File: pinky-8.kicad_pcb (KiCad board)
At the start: 2 copper layers, 91.4 x 68.6 mm, 21 parts, among them P1 USB_B, P2 PERIPHERAL A, P3 PERIPHERAL B, P4 2x3 HEADER, U1 W65C02S, U2 74AC00, U3 AS6C62256, U4 DS1813, U5 GLS29EE010, U6 W65C22S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

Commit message: Updating to Rev B spec.
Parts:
- removed C2: 100uF, Capacitors_THT:CP_Radial_D6.3mm_P2.50mm
- removed the G*** at (118.1, 66.0)
- removed R4, R5: 3.3K, Resistors_THT:R_Axial_DIN0204_L3.6mm_D1.6mm_P7.62mm_Horizontal
- removed the REF** at (110.5, 123.2)
- removed the REF** at (191.8, 81.3)
- removed the REF** at (110.5, 64.8)
- removed U1: W65C02S, Housings_DIP:DIP-40_W15.24mm_LongPads
- removed U2: 74AC00, Housings_DIP:DIP-14_W7.62mm_LongPads
- removed U3: AS6C62256, Housings_DIP:DIP-28_W15.24mm_LongPads
- removed U4: DS1813, TO_SOT_Packages_THT:TO-92_Inline_Wide
- removed U5: GLS29EE010, Housings_DIP:DIP-32_W15.24mm_Socket_LongPads
- removed X1: MXO45, Housings_DIP:DIP-8_W7.62mm_Socket_LongPads
- added B0: CONN_01X03, Pin_Headers:Pin_Header_Straight_1x03_Pitch2.54mm, F.Cu at (139.7, 31.8)
- added B1: CONN_01X03, Pin_Headers:Pin_Header_Straight_1x03_Pitch2.54mm, F.Cu at (135.9, 31.8)
- added B2: CONN_01X03, Pin_Headers:Pin_Header_Straight_1x03_Pitch2.54mm, F.Cu at (132.1, 31.8)
- added C7: 100uF, Capacitors_THT:CP_Radial_D6.3mm_P2.50mm, F.Cu at (157.5, 31.8)
- added CPU: W65C02S, Housings_DIP:DIP-40_W15.24mm_LongPads, F.Cu at (113.0, 44.5)
- added DEC: 74AC00, Housings_DIP:DIP-14_W7.62mm_LongPads, F.Cu at (132.1, 49.5)
- added G***: OSHW-logo_silkscreen-front_8mm, OSHW-logo:OSHW-logo_silkscreen-front_8mm, F.Cu at (87.0, 62.2)
- added NMI: SW_Push_Dual, Buttons_Switches_THT:SW_TH_Tactile_Omron_B3F-10xx, F.Cu at (101.6, 30.5)
- added OSC: MXO45, Housings_DIP:DIP-8_W7.62mm_Socket_LongPads, F.Cu at (114.3, 30.5)
- added P10: CONN_01X01, Wire_Pads:SolderWirePad_single_0-8mmDrill, F.Cu at (135.3, 92.1)
- added P11: CONN_01X01, Wire_Pads:SolderWirePad_single_0-8mmDrill, F.Cu at (154.3, 87.6)
- added P13: CONN_01X01, Wire_Pads:SolderWirePad_single_0-8mmDrill, F.Cu at (124.5, 91.4)
- added P14: CONN_01X01, Wire_Pads:SolderWirePad_single_0-8mmDrill, F.Cu at (144.1, 54.0)
- added P15: CONN_01X01, Wire_Pads:SolderWirePad_single_0-8mmDrill, F.Cu at (116.8, 61.0)
- added P17: CONN_01X01, Wire_Pads:SolderWirePad_single_0-8mmDrill, F.Cu at (97.2, 44.5)
- added P5: CONN_01X01, Wire_Pads:SolderWirePad_single_0-8mmDrill, F.Cu at (147.3, 46.4)
- added P6: CONN_01X01, Wire_Pads:SolderWirePad_single_0-8mmDrill, F.Cu at (163.2, 54.6)
- added PA: PERIPHERAL A, Socket_Strips:Socket_Strip_Straight_2x07_Pitch2.54mm, F.Cu at (87.6, 36.8)
- added PB: PERIPHERAL B, Socket_Strips:Socket_Strip_Straight_2x07_Pitch2.54mm, F.Cu at (87.6, 72.4)
- added R3: 3.3K, Resistors_THT:R_Axial_DIN0204_L3.6mm_D1.6mm_P7.62mm_Horizontal, F.Cu at (128.3, 38.1)
- added RAM: AS6C62256, Housings_DIP:DIP-28_W15.24mm_LongPads, F.Cu at (166.4, 87.6)
- added REF**: MountingHole_2.7mm_M2.5, Mounting_Holes:MountingHole_2.7mm_M2.5, F.Cu at (165.7, 31.1)
- added REF**: MountingHole_2.7mm_M2.5, Mounting_Holes:MountingHole_2.7mm_M2.5, F.Cu at (165.7, 93.3)
- added REF**: MountingHole_2.7mm_M2.5, Mounting_Holes:MountingHole_2.7mm_M2.5, F.Cu at (85.7, 93.3)
- added REF**: MountingHole_2.7mm_M2.5, Mounting_Holes:MountingHole_2.7mm_M2.5, F.Cu at (85.7, 31.1)
- added ROM: GLS29EE010, Housings_DIP:DIP-32_W15.24mm_Socket_LongPads, F.Cu at (147.3, 92.7)
- added U7: DS1813, TO_SOT_Packages_THT:TO-92_Inline_Wide, F.Cu at (151.1, 35.6)
- added USB-B: USB_B, Connectors:USB_B, F.Cu at (154.9, 43.2)
- added VIA: W65C22S, Housings_DIP:DIP-40_W15.24mm_LongPads, F.Cu at (94.0, 44.5)
- P1: value USB_B -> CONN_01X01; footprint Connectors:USB_B -> Wire_Pads:SolderWirePad_single_0-8mmDrill
- P2: value PERIPHERAL A -> CONN_01X01; footprint Socket_Strips:Socket_Strip_Straight_2x07_Pitch2.54mm -> Wire_Pads:SolderWirePad_single_0-8mmDrill
- P3: value PERIPHERAL B -> CONN_01X01; footprint Socket_Strips:Socket_Strip_Straight_2x07_Pitch2.54mm -> Wire_Pads:SolderWirePad_single_0-8mmDrill
- P4: value 2x3 HEADER -> CONN_01X01; footprint Pin_Headers:Pin_Header_Straight_2x03_Pitch2.54mm -> Wire_Pads:SolderWirePad_single_0-8mmDrill
- U6: value W65C22S -> DS1813; footprint Housings_DIP:DIP-40_W15.24mm_LongPads -> TO_SOT_Packages_THT:TO-92_Inline_Wide
- moved P1 77.8 mm to (118.1, 30.5)
- moved P4 75.4 mm to (118.1, 38.1), turned to 0 degrees
- moved R1 60.2 mm to (110.5, 30.5), turned to 270 degrees
- moved U6 41.9 mm to (106.7, 35.6), turned to 90 degrees
- moved RESET 40.2 mm to (147.3, 30.5), turned to 270 degrees
- moved P2 34.0 mm to (132.1, 45.1)
- moved R2 29.0 mm to (125.7, 38.1), turned to 90 degrees
- moved P3 16.5 mm to (97.2, 92.7)
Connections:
- P4 pad 1: Net-(P4-Pad1) -> GND
- R1 pad 1: Net-(R1-Pad1) -> VCC
- R1 pad 2: VCC -> Net-(R1-Pad2)
- R2 pad 1: VCC -> /PLUP
- R2 pad 2: Net-(R2-Pad2) -> VCC
- RESET pad 4: /RST -> /RST#
- U6 pad 1: GND -> /NMI#
- U6 pad 2: /PA0 -> VCC
- U6 pad 3: /PA1 -> GND
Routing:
- net /RW#: track 0.00 -> 124.9 mm, vias 0 -> 5
- net /RB2: track 0.00 -> 88.2 mm, vias 0 -> 1
- net /RW: track 83.6 -> 0.00 mm, vias 1 -> 0
- net /CLK: track 17.6 -> 99.5 mm
- net /VIASEL: track 78.7 -> 0.00 mm, vias 2 -> 0
- net /VIASEL#: track 0.00 -> 75.6 mm, vias 0 -> 2
- net /PHI2: track 65.7 -> 0.00 mm
- net /RST#: track 0.00 -> 59.7 mm, vias 0 -> 1
- net /ROMSEL#: track 0.00 -> 58.8 mm, vias 0 -> 2
- net /IRQ#: track 0.00 -> 57.8 mm, vias 0 -> 1
- net /RST: track 56.1 -> 0.00 mm, vias 3 -> 0
- net /IRQ: track 54.6 -> 0.00 mm
- net /ROMSEL: track 53.1 -> 0.00 mm
- net Net-(R2-Pad2): track 47.7 -> 0.00 mm, vias 1 -> 0
- net /NMI#: track 0.00 -> 40.1 mm, vias 0 -> 1
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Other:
- board size 91.4 x 68.6 mm -> 88.9 x 71.1 mm
- net class Power added: clearance 0.25, trace_width 0.38, via_dia 0.4, via_drill 0.3
- rule pad_to_mask_clearance: 0.2 -> 0
- rule trace_min: 0.1524 -> 0.2
- board text added: "(C) 2017 Auston Stewart"
- board text added: "PINKY-8 (REV B)"
- board text added: "github.com/contrarian-computing"
- board text removed: "0"
- board text removed: "1"
- board text removed: "B0"
- board text removed: "B1"
- board text removed: "PINKY-8 (REV A) (C) 2017 Auston Stewart"
- board text removed: "contrariancomputing.net"

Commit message: Reducing data line trace overlap.
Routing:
- net /D1: track 62.1 -> 66.1 mm, vias 1 -> 2
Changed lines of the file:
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@@
     (thickness 1.6)
     (drawings 13)
-    (tracks 725)
+    (tracks 723)
     (zones 0)
     (modules 37)
@@
   (segment (start 110.49 59.69) (end 111.76 58.42) (width 0.25) (layer F.Cu) (net 29))
   (segment (start 111.76 58.42) (end 115.57 58.42) (width 0.25) (layer F.Cu) (net 29))
-  (segment (start 124.46 44.45) (end 128.27 44.45) (width 0.25) (layer B.Cu) (net 29) (status 800000))
+  (segment (start 124.46 44.45) (end 128.27 44.45) (width 0.25) (layer B.Cu) (net 29))
   (via (at 124.46 44.45) (size 0.6) (drill 0.4) (layers F.Cu B.Cu) (net 29))
   (segment (start 151.13 35.56) (end 144.78 35.56) (width 0.25) (layer F.Cu) (net 29))
@@
   (segment (start 128.27 40.64) (end 129.54 39.37) (width 0.25) (layer F.Cu) (net 29))
   (segment (start 142.82 37.52) (end 142.82 36.98) (width 0.25) (layer F.Cu) (net 29))
-  (segment (start 142.24 41.91) (end 142.24 43.18) (width 0.25) (layer B.Cu) (net 32) (status 400000))
-  (segment (start 137.16 43.18) (end 137.16 41.91) (width 0.25) (layer B.Cu) (net 32) (status 800000))
+  (segment (start 142.24 41.91) (end 142.24 43.18) (width 0.25) (layer B.Cu) (net 32))
+  (segment (start 137.16 43.18) (end 137.16 41.91) (width 0.25) (layer B.Cu) (net 32))
   (segment (start 138.43 44.45) (end 137.16 43.18) (width 0.25) (layer B.Cu) (net 32))
   (segment (start 140.97 44.45) (end 138.43 44.45) (width 0.25) (layer B.Cu) (net 32))
   (segment (start 142.24 43.18) (end 140.97 44.45) (width 0.25) (layer B.Cu) (net 32))
-  (segment (start 144.78 41.91) (end 142.24 41.91) (width 0.25) (layer B.Cu) (net 32) (status C00000))
+  (segment (start 144.78 41.91) (end 142.24 41.91) (width 0.25) (layer B.Cu) (net 32))
   (segment (start 144.78 41.91) (end 144.78 43.18) (width 0.25) (layer F.Cu) (net 32))
   (segment (start 158.75 57.15) (end 158.75 77.47) (width 0.25) (layer F.Cu) (net 32))
@@
   (segment (start 129.54 90.17) (end 130.81 91.44) (width 0.25) (layer F.Cu) (net 34))
   (segment (start 138.43 57.15) (end 142.24 57.15) (width 0.25) (layer B.Cu) (net 35))
-  (segment (start 149.86 57.15) (end 151.13 57.15) (width 0.25) (layer F.Cu) (net 35) (status 800000))
+  (segment (start 149.86 57.15) (end 151.13 57.15) (width 0.25) (layer F.Cu) (net 35))
   (segment (start 148.59 58.42) (end 149.86 57.15) (width 0.25) (layer F.Cu) (net 35))
   (segment (start 143.51 58.42) (end 148.59 58.42) (width 0.25) (layer F.Cu) (net 35))
@@
   (segment (start 135.89 78.74) (end 148.59 78.74) (width 0.25) (layer B.Cu) (net 52))
   (segment (start 134.62 80.01) (end 135.89 78.74) (width 0.25) (layer B.Cu) (net 52))
+  (segment (start 134.62 60.96) (end 125.73 60.96) (width 0.25) (layer B.Cu) (net 53))
+  (segment (start 147.32 59.69) (end 135.89 59.69) (width 0.25) (layer B.Cu) (net 53))
+  (segment (start 134.62 60.96) (end 135.89 59.69) (width 0.25) (layer B.Cu) (net 53))
+  (via (at 125.73 64.77) (size 0.6) (drill 0.4) (layers F.Cu B.Cu) (net 53))
+  (segment (start 125.73 60.96) (end 125.73 64.77) (width 0.25) (layer F.Cu) (net 53))
+  (via (at 125.73 60.96) (size 0.6) (drill 0.4) (layers F.Cu B.Cu) (net 53))
   (segment (start 128.27 64.77) (end 125.73 64.77) (width 0.25) (layer B.Cu) (net 53))
   (segment (start 110.49 64.77) (end 109.22 64.77) (width 0.25) (layer B.Cu) (net 53))
+  (segment (start 125.73 64.77) (end 124.46 63.5) (width 0.25) (layer B.Cu) (net 53))
+  (segment (start 124.46 63.5) (end 111.76 63.5) (width 0.25) (layer B.Cu) (net 53))
   (segment (start 111.76 63.5) (end 110.49 64.77) (width 0.25) (layer B.Cu) (net 53))
-  (segment (start 124.46 63.5) (end 111.76 63.5) (width 0.25) (layer B.Cu) (net 53))
-  (segment (start 125.73 64.77) (end 124.46 63.5) (width 0.25) (layer B.Cu) (net 53))
-  (segment (start 128.27 64.77) (end 129.54 64.77) (width 0.25) (layer F.Cu) (net 53))
-  (segment (start 133.35 63.5) (end 134.62 62.23) (width 0.25) (layer F.Cu) (net 53))
-  (segment (start 134.62 62.23) (end 134.62 60.96) (width 0.25) (layer F.Cu) (net 53))
-  (via (at 134.62 60.96) (size 0.6) (drill 0.4) (layers F.Cu B.Cu) (net 53))
-  (segment (start 134.62 60.96) (end 135.89 59.69) (width 0.25) (layer B.Cu) (net 53))
-  (segment (start 135.89 59.69) (end 147.32 59.69) (width 0.25) (layer B.Cu) (net 53))
-  (segment (start 130.81 63.5) (end 133.35 63.5) (width 0.25) (layer F.Cu) (net 53))
-  (segment (start 129.54 64.77) (end 130.81 63.5) (width 0.25) (layer F.Cu) (net 53))
   (segment (start 147.32 59.69) (end 148.59 59.69) (width 0.25) (layer B.Cu) (net 53))
   (segment (start 163.83 59.69) (end 166.37 59.69) (width 0.25) (layer B.Cu) (net 53))
@@
   (segment (start 135.89 55.88) (end 142.24 55.88) (width 0.25) (layer B.Cu) (net 55))
   (segment (start 128.27 67.31) (end 129.54 67.31) (width 0.25) (layer F.Cu) (net 55))
-  (segment (start 143.51 57.15) (end 147.32 57.15) (width 0.25) (layer B.Cu) (net 55) (status 800000))
+  (segment (start 143.51 57.15) (end 147.32 57.15) (width 0.25) (layer B.Cu) (net 55))
   (segment (start 109.22 67.31) (end 110.49 67.31) (width 0.25) (layer B.Cu) (net 55))
   (segment (start 125.73 67.31) (end 128.27 67.31) (width 0.25) (layer B.Cu) (net 55))
@@
   (segment (start 111.76 88.9) (end 115.57 88.9) (width 0.25) (layer B.Cu) (net 56))
   (segment (start 110.49 90.17) (end 111.76 88.9) (width 0.25) (layer B.Cu) (net 56))
-  (segment (start 139.7 41.91) (end 139.7 45.72) (width 0.25) (layer F.Cu) (net 58) (status 400000))
+  (segment (start 139.7 41.91) (end 139.7 45.72) (width 0.25) (layer F.Cu) (net 58))
   (segment (start 144.78 62.23) (end 138.43 55.88) (width 0.25) (layer F.Cu) (net 58))
   (segment (start 144.78 62.23) (end 144.78 66.04) (width 0.25) (layer F.Cu) (net 58))
@@
   (segment (start 100.33 86.36) (end 100.33 53.34) (width 0.25) (layer F.Cu) (net 62))
   (segment (start 106.68 92.71) (end 100.33 86.36) (width 0.25) (layer F.Cu) (net 62))
-  (segment (start 134.62 49.53) (end 132.08 49.53) (width 0.25) (layer B.Cu) (net 64) (status C00000))
+  (segment (start 134.62 49.53) (end 132.08 49.53) (width 0.25) (layer B.Cu) (net 64))
   (segment (start 134.62 49.53) (end 134.62 58.42) (width 0.25) (layer F.Cu) (net 64))
   (via (at 124.46 58.42) (size 0.6) (drill 0.4) (layers F.Cu B.Cu) (net 64))
@@
   (segment (start 111.76 86.36) (end 115.57 86.36) (width 0.25) (layer B.Cu) (net 69))
   (segment (start 110.49 87.63) (end 111.76 86.36) (width 0.25) (layer B.Cu) (net 69))
-  (segment (start 139.7 49.53) (end 137.16 49.53) (width 0.25) (layer B.Cu) (net 70) (status C00000))
+  (segment (start 139.7 49.53) (end 137.16 49.53) (width 0.25) (layer B.Cu) (net 70))
   (segment (start 125.73 38.1) (end 132.08 31.75) (width 0.25) (layer F.Cu) (net 72))
   (segment (start 135.89 31.75) (end 139.7 31.75) (width 0.25) (layer F.Cu) (net 72))

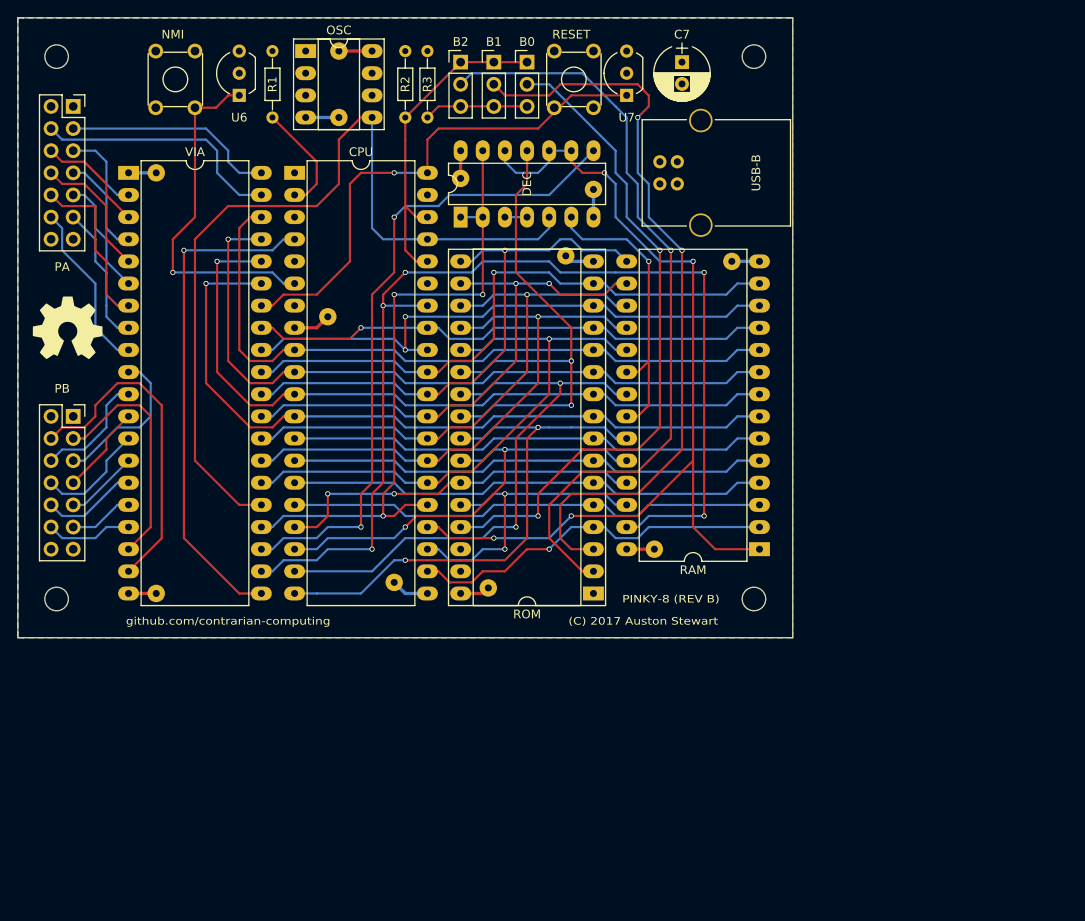
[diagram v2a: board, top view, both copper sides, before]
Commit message: Finalizing PCB layout and updating schematic.
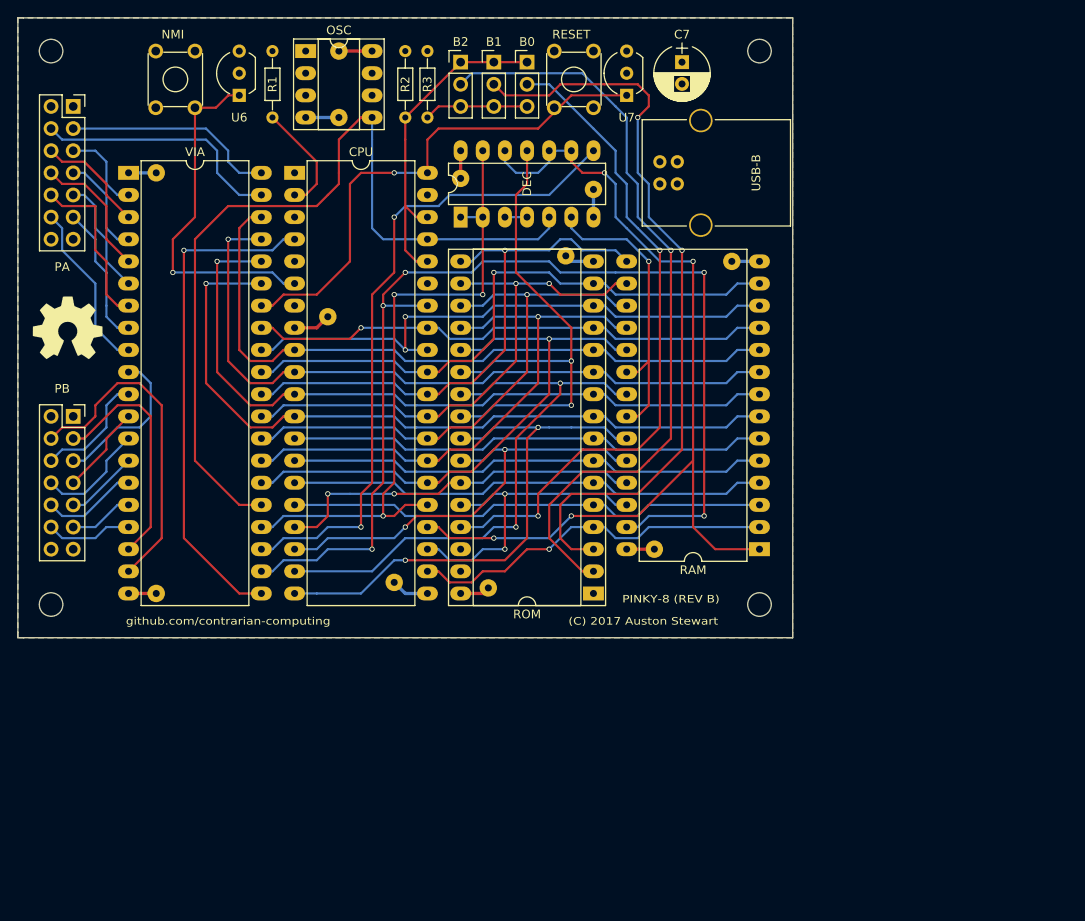
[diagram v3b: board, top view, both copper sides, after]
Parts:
- moved REF** 0.90 mm to (166.4, 94.0)
- moved REF** 0.90 mm to (85.1, 94.0)
- moved REF** 0.90 mm to (166.4, 30.5)
- moved REF** 0.90 mm to (85.1, 30.5)
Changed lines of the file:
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@@
   )
   (module Mounting_Holes:MountingHole_2.7mm_M2.5 (layer F.Cu)
-    (at 165.735 31.115)
+    (at 166.37 30.48)
     (descr "Mounting Hole 2.7mm, no annular, M2.5")
     (tags "mounting hole 2.7mm no annular m2.5")
@@
   )
   (module Mounting_Holes:MountingHole_2.7mm_M2.5 (layer F.Cu)
-    (at 165.735 93.345)
+    (at 166.37 93.98)
     (descr "Mounting Hole 2.7mm, no annular, M2.5")
     (tags "mounting hole 2.7mm no annular m2.5")
@@
   )
   (module Mounting_Holes:MountingHole_2.7mm_M2.5 (layer F.Cu)
-    (at 85.725 93.345)
+    (at 85.09 93.98)
     (descr "Mounting Hole 2.7mm, no annular, M2.5")
     (tags "mounting hole 2.7mm no annular m2.5")
@@
   )
   (module Mounting_Holes:MountingHole_2.7mm_M2.5 (layer F.Cu)
-    (at 85.725 31.115)
+    (at 85.09 30.48)
     (descr "Mounting Hole 2.7mm, no annular, M2.5")
     (tags "mounting hole 2.7mm no annular m2.5")

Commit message: Fixing a routing error
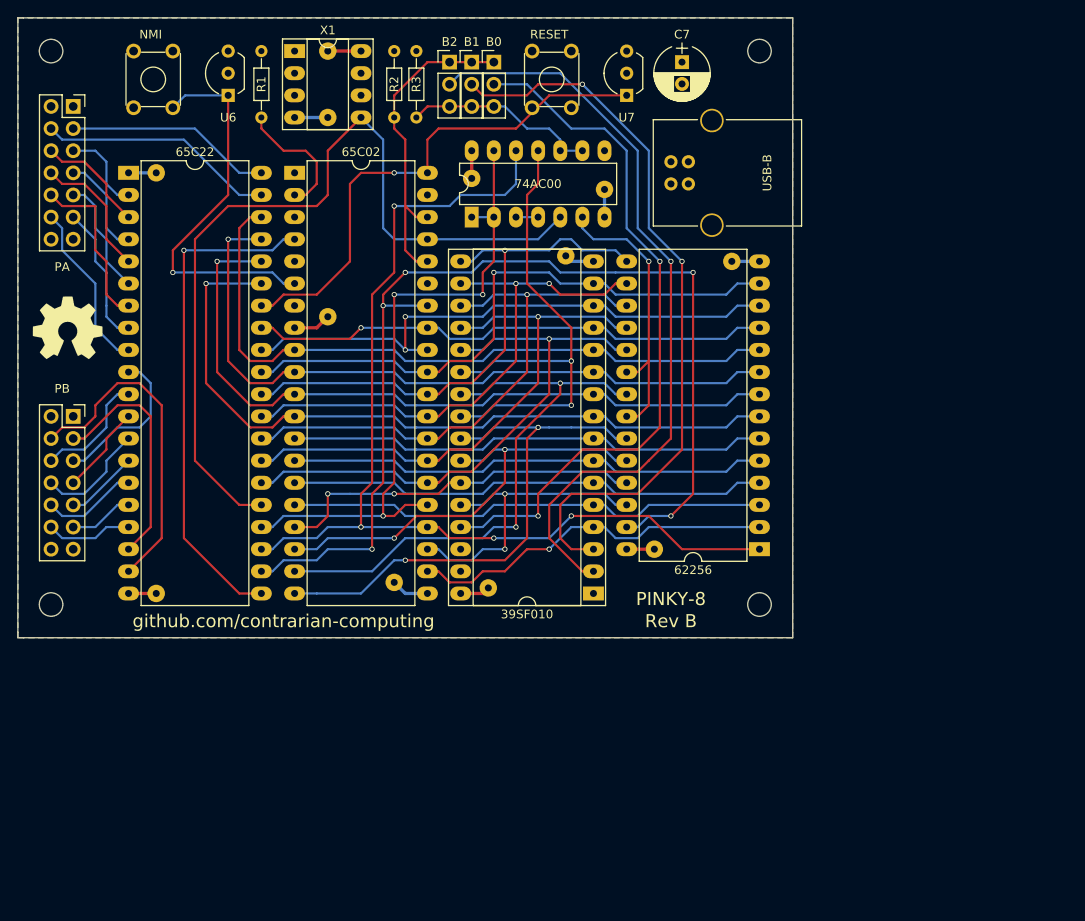
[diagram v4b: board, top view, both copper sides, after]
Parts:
- moved B0 3.81 mm to (135.9, 31.8)
- moved B1 2.54 mm to (133.3, 31.8)
- moved NMI 2.54 mm to (99.1, 30.5)
- moved RESET 2.54 mm to (144.8, 30.5)
- moved B2 1.27 mm to (130.8, 31.8)
- moved P5 1.27 mm to (148.6, 46.4)
- moved R2 1.27 mm to (124.5, 38.1)
- moved R3 1.27 mm to (127.0, 38.1)
- moved U6 1.27 mm to (105.4, 35.6)
- moved USB-B 1.27 mm to (156.2, 43.2)
- moved P1 1.27 mm to (116.8, 30.5)
- moved P4 1.27 mm to (116.8, 38.1)
- moved R1 1.27 mm to (109.2, 30.5)
- moved X1 1.27 mm to (113.0, 30.5)
- moved 74AC00 1.27 mm to (133.3, 49.5)
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- renumbered ROM to 39SF010, RAM to 62256, CPU to 65C02, VIA to 65C22, DEC to 74AC00, OSC to X1
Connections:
- 65C22 pad 23: /VIASEL# -> /A14
- 74AC00 pad 10: /A14 -> /PLDN
- 74AC00 pad 8: /VIASEL# -> Net-(U4-Pad8)
- 74AC00 pad 9: /A14 -> /PLDN
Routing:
- net /VIASEL#: track 75.6 -> 0.00 mm, vias 2 -> 0
- net /A14: track 107.3 -> 118.6 mm
- net /PLDN: track 12.0 -> 22.4 mm
- net /RB0: track 76.3 -> 80.8 mm
- net /NMI#: track 40.1 -> 44.4 mm
- net /RW#: track 124.9 -> 120.8 mm
- net /RB1: track 87.4 -> 85.1 mm
- net Net-(R1-Pad2): track 12.8 -> 14.8 mm
- net /CA2: track 28.8 -> 27.3 mm
- net /RAMSEL#: track 34.4 -> 33.1 mm
- net /CLK: track 99.5 -> 98.6 mm
- net /CA1: track 24.4 -> 23.7 mm
- net /PLUP: track 38.0 -> 37.4 mm
- net /A15: track 75.2 -> 75.8 mm
- net /ROMSEL#: track 58.8 -> 58.3 mm
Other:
- board text added: "PINKY-8"
- board text added: "Rev B"
- board text removed: "(C) 2017 Auston Stewart"
- board text removed: "PINKY-8 (REV B)"
